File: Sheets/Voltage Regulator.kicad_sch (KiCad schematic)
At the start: 8 parts, among them IC201 LM2678SX-5.0

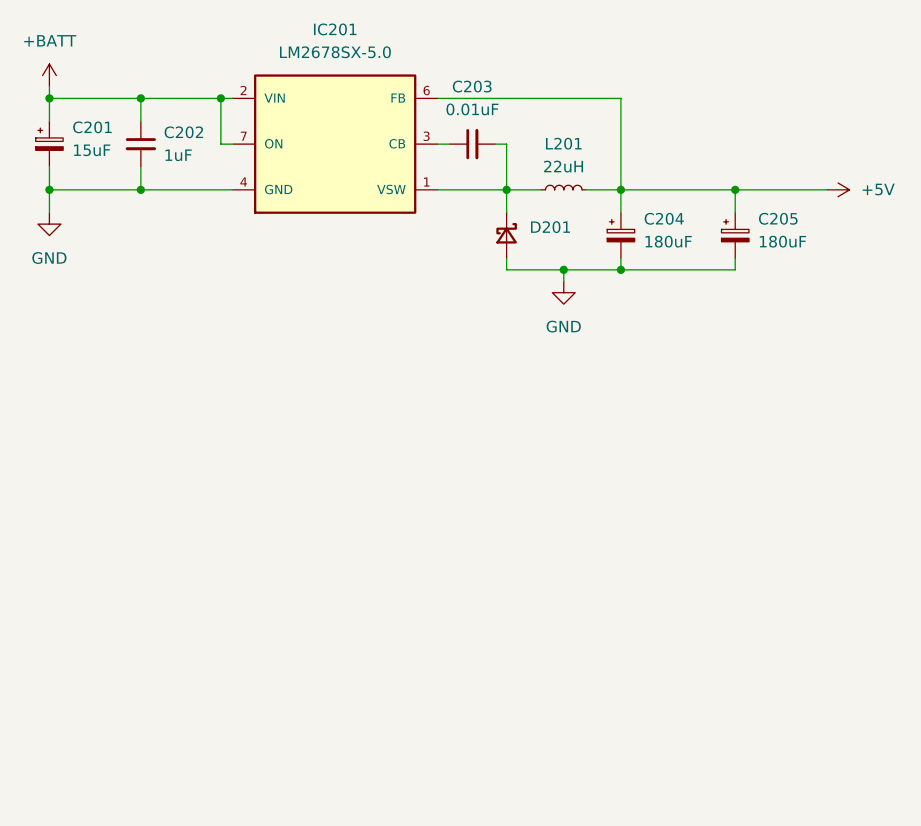
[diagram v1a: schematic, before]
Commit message: Rev 1.2 Add 12v buck converter
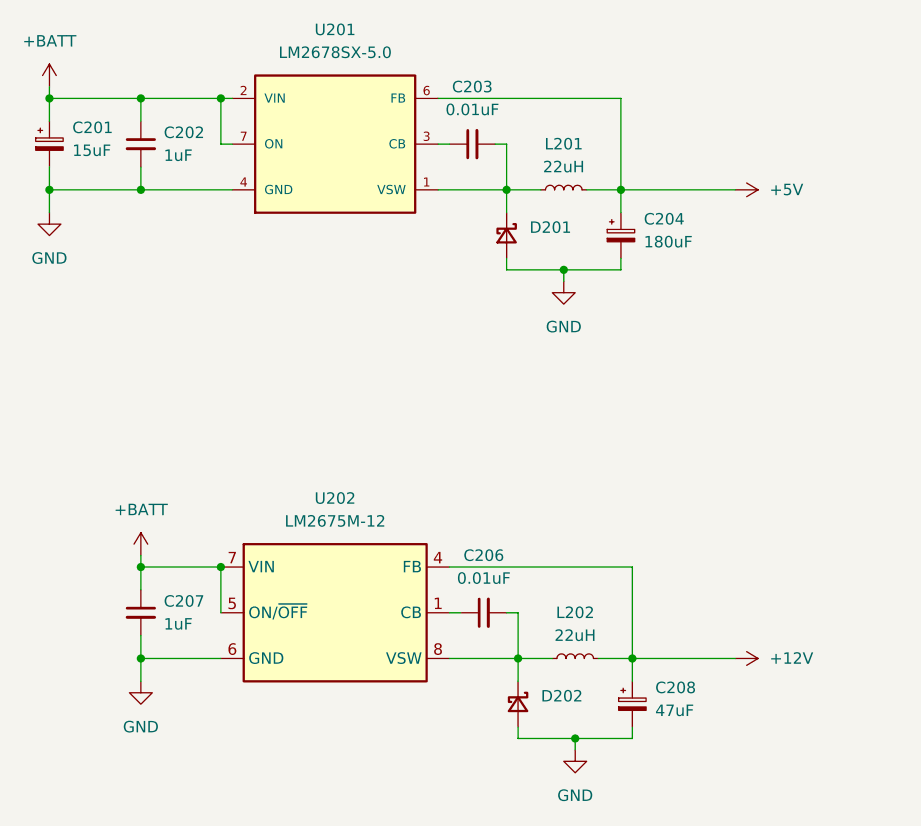
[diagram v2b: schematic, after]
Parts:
- removed C205: 180uF, Capacitor_THT:CP_Radial_D8.0mm_P3.50mm, symbol Device:C_Polarized_Small
- added C206: 0.01uF, Capacitor_SMD:C_1206_3216Metric_Pad1.33x1.80mm_HandSolder, symbol Device:C_Small
- added C207: 1uF, Capacitor_SMD:C_1206_3216Metric_Pad1.33x1.80mm_HandSolder, symbol Device:C_Small
- added C208: 47uF, Capacitor_SMD:C_1206_3216Metric_Pad1.33x1.80mm_HandSolder, symbol Device:C_Polarized_Small
- added D202: ~, Diode_THT:D_DO-41_SOD81_P10.16mm_Horizontal, symbol Device:D_Schottky_Small
- added L202: 22uH, Inductor_SMD:L_6.3x6.3_H3, symbol Device:L_Small
- added U202: LM2675M-12, Package_SO:SOIC-8_3.9x4.9mm_P1.27mm, symbol Regulator_Switching:LM2675M-12
- renumbered IC201 to U201
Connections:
- net +BATT: now also C207.1, U202.5 (ON/~{OFF}), U202.7 (VIN)
- net GND: now also C207.2, C208.2, D202.2 (A), U202.6 (GND)
- new net: C206.2, D202.1 (K), L202.1, U202.8 (VSW)
- new net: C206.1, U202.1 (CB)
- new net +12V: C208.1, L202.2, U202.4 (FB)
